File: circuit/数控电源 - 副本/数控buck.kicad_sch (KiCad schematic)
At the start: 78 parts, among them J1 Conn_01x06_MountingPin, J2 Conn_01x02, J5 Conn_01x02, Q1 BSC070N10NS3G, Q2 BSC070N10NS3G, SW1 SW_Push, U1 STM32F334R8Tx, U2 LM5164DDA, U3 TLV9062, U4 LM5109MA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

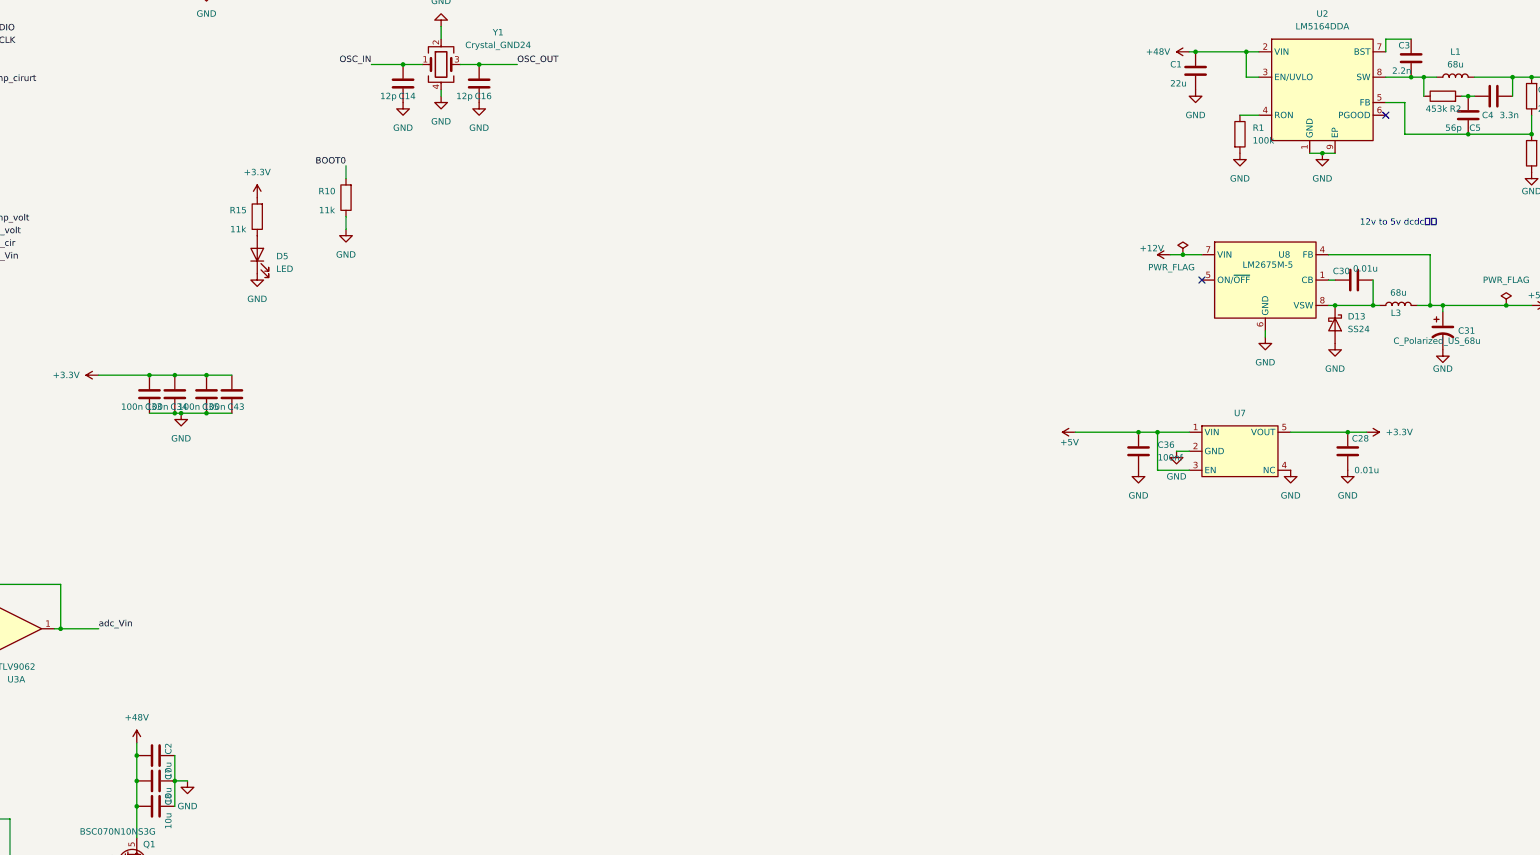
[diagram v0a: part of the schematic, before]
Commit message: 重新对第二版pcb进行布局
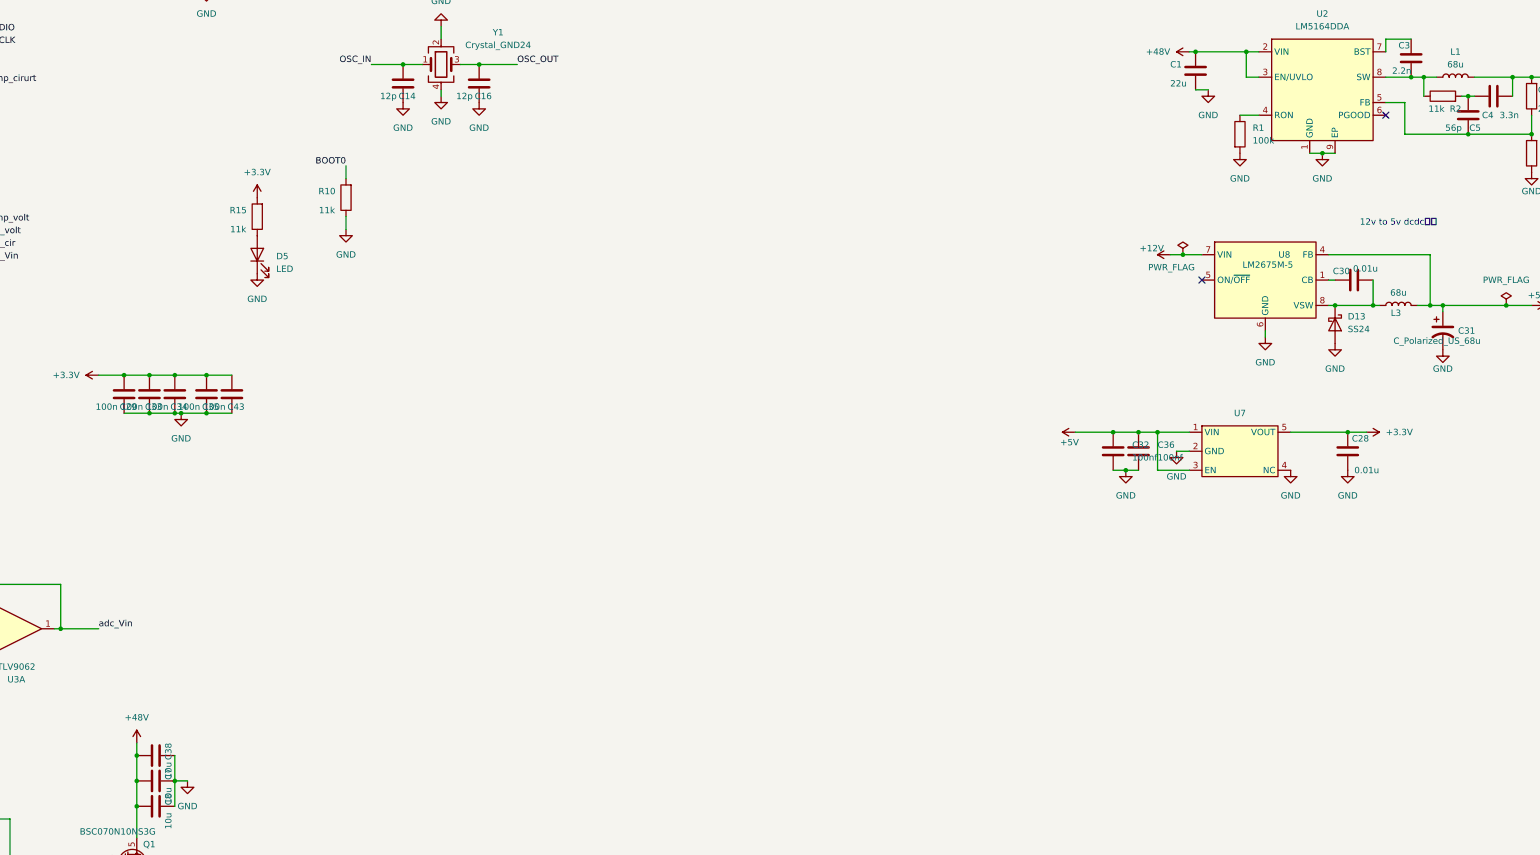
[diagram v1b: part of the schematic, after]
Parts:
- removed C2: 10u, Capacitor_SMD:C_1210_3225Metric, symbol Device:C
- added C29: 100n, Capacitor_SMD:C_0603_1608Metric, symbol Device:C
- added C32: 100nf, Capacitor_SMD:C_0603_1608Metric, symbol Device:C
- added C38: 10u, Capacitor_SMD:C_1210_3225Metric, symbol Device:C
- J2: footprint Connector_AMASS:AMASS_XT30PW-M_1x02_P2.50mm_Horizontal -> Connector_AMASS:AMASS_XT30U-M_1x02_P5.0mm_Vertical
- J5: footprint Connector_AMASS:AMASS_XT30PW-F_1x02_P2.50mm_Horizontal -> Connector_AMASS:AMASS_XT30U-F_1x02_P5.0mm_Vertical
- R2: value 453k -> 11k
- U2: footprint Package_SO:HSOP-8-1EP_3.9x4.9mm_P1.27mm_EP2.41x3.1mm -> Package_SO:HSOP-8-1EP_3.9x4.9mm_P1.27mm_EP2.41x3.1mm_ThermalVias
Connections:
- net +3.3V: now also C29.2
- net +48V: now also C38.2
- net +5V: now also C32.1
- net GND: now also C29.1, C32.2, C38.1
